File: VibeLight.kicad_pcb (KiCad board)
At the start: 2 copper layers, 29 x 34 mm, 36 parts, among them SW1 SW_Push, SW2 SW_Push, U2 SPV08A0LR5H-1, U3 BL652

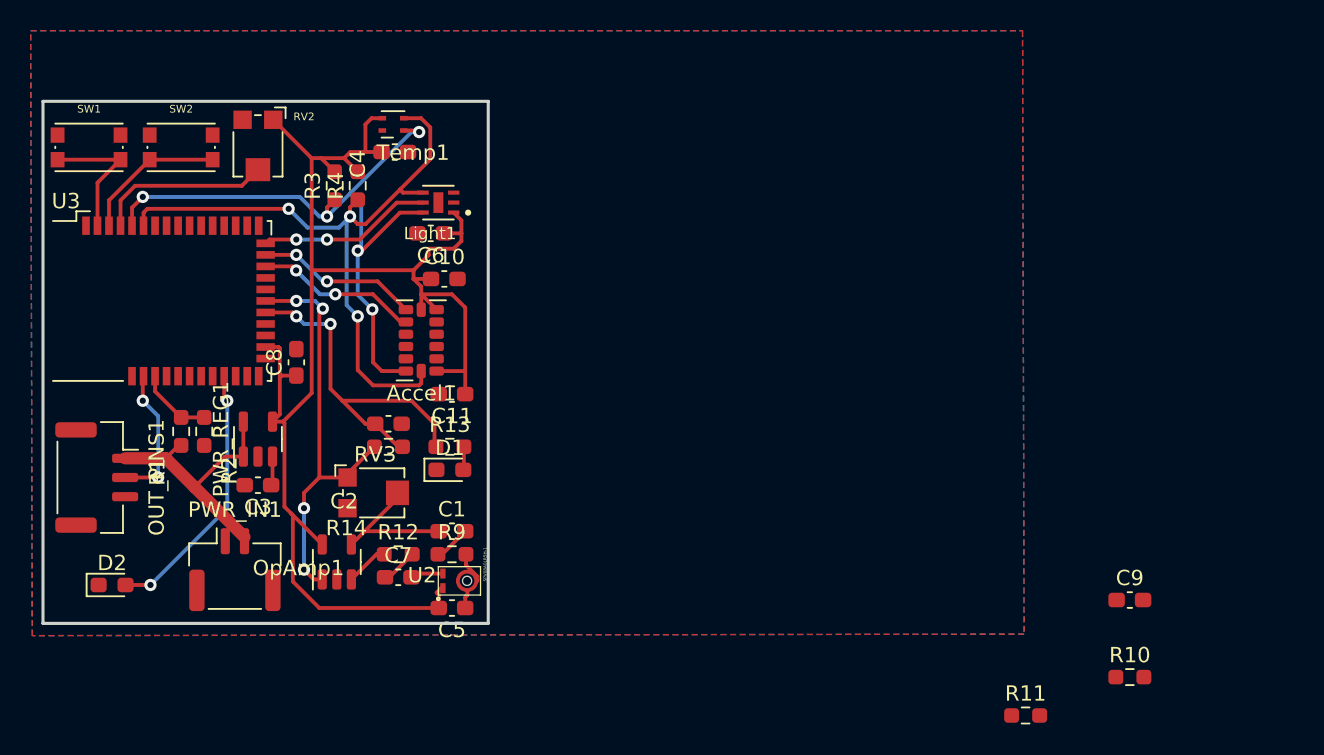
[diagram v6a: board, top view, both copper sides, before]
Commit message: new pcb rev with updated audio filter
The only ERC and DRC warnings/errors are unconnected pins and silkscreen text issues. There are two DRC issues that have to do with the mic, but I don't think they're an issue
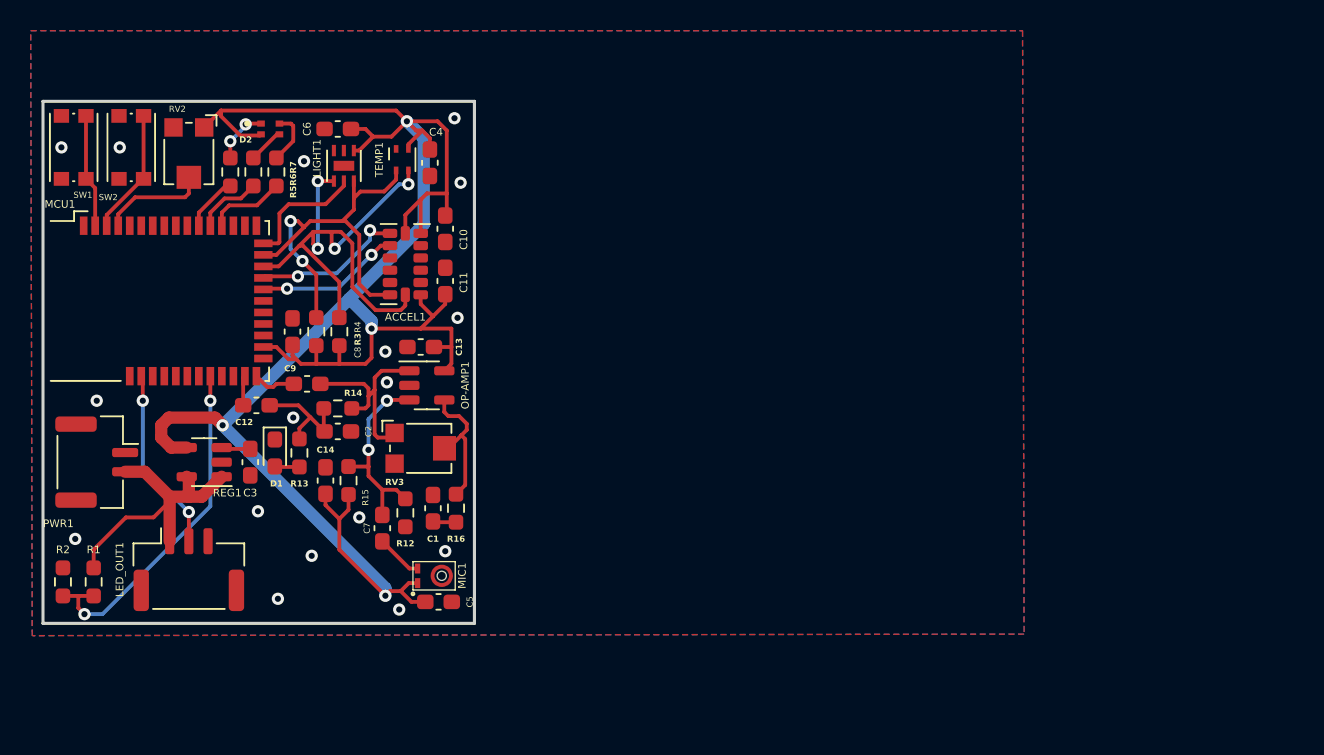
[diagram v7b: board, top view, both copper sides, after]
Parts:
- removed OpAmp1: AD8603, Package_TO_SOT_SMD:TSOT-23-5
- removed R10, R11: 10K, Resistor_SMD:R_0603_1608Metric_Pad0.98x0.95mm_HandSolder
- removed R9: R, Resistor_SMD:R_0603_1608Metric_Pad0.98x0.95mm_HandSolder
- removed U2: SPV08A0LR5H-1, MEMS_Mic_SMD:SPV08A0LR5H-1
- added C12: 100 nF, Capacitor_SMD:C_0603_1608Metric_Pad1.08x0.95mm_HandSolder, F.Cu at (31.9, 38.8)
- added C13: 100 nF, Capacitor_SMD:C_0603_1608Metric_Pad1.08x0.95mm_HandSolder, F.Cu at (42.6, 35.0)
- added C14: 100 nF, Capacitor_SMD:C_0603_1608Metric_Pad1.08x0.95mm_HandSolder, F.Cu at (36.4, 43.7)
- added MIC1: SPV08A0LR5H-1, MEMS_Mic_SMD:SPV08A0LR5H-1, F.Cu at (44.0, 49.9)
- added OP-AMP1: AD8603, Package_TO_SOT_SMD:TSOT-23-5, F.Cu at (43.0, 37.5)
- added R15: 10K, Resistor_SMD:R_0603_1608Metric_Pad0.98x0.95mm_HandSolder, F.Cu at (37.9, 43.7)
- added R16: 10K, Resistor_SMD:R_0603_1608Metric_Pad0.98x0.95mm_HandSolder, F.Cu at (44.9, 45.5)
- added R5: 100R, Resistor_SMD:R_0603_1608Metric_Pad0.98x0.95mm_HandSolder, F.Cu at (30.2, 23.6)
- added R6: 100R, Resistor_SMD:R_0603_1608Metric_Pad0.98x0.95mm_HandSolder, F.Cu at (31.7, 23.6)
- added R7: 100R, Resistor_SMD:R_0603_1608Metric_Pad0.98x0.95mm_HandSolder, F.Cu at (33.2, 23.6)
- C1: value C -> 100 nF
- C7: value 4.7uF -> 1 uF
- C9: value 1uF -> 100 nF
- D2: value LED -> LED_RBAG; footprint LED_SMD:LED_0603_1608Metric_Pad1.05x0.95mm_HandSolder -> RBG_LED:LED_APHB1608LZGKSURKC
- R12: value 4.7K -> 10K
- R13: value 60R -> 100R
- moved C9 55.4 mm to (35.2, 37.4), turned to 180 degrees
- moved D2 31.4 mm to (32.8, 20.8)
- moved R2 13.4 mm to (19.3, 50.3), turned to 90 degrees
- moved D1 11.5 mm to (33.1, 41.9), turned to -90 degrees
- moved PWR1 11.4 mm to (21.5, 42.5), turned to -90 degrees
- moved R1 11.3 mm to (21.3, 50.3), turned to -90 degrees
- moved R13 9.81 mm to (34.7, 41.9), turned to -90 degrees
- moved R3 9.58 mm to (35.8, 34.0), turned to -90 degrees
- moved R4 9.58 mm to (37.3, 34.0), turned to -90 degrees
- moved C6 9.10 mm to (37.2, 20.8)
- moved LED_OUT1 8.49 mm to (27.5, 49.5), turned to 0 degrees
- moved C11 7.38 mm to (44.2, 30.7), turned to 90 degrees
- moved LIGHT1 6.60 mm to (37.6, 23.2), turned to -90 degrees
- moved ACCEL1 5.08 mm to (41.6, 29.6)
- moved RV2 4.53 mm to (27.5, 22.5)
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- renumbered Accel1 to ACCEL1, OUT_PINS1 to LED_OUT1, Light1 to LIGHT1, U3 to MCU1, PWR_IN1 to PWR1, PWR_REG1 to REG1, Temp1 to TEMP1
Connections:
- C1 pad 1: Net-(OpAmp1--) -> GND
- C2 pad 2: /Audio Input/FIL -> Net-(C12-Pad1)
- C7 pad 1: Net-(C7-Pad1) -> Net-(OP-AMP1-+)
- C9 pad 1: GND -> Net-(C9-Pad1)
- C9 pad 2: Net-(OpAmp1-+) -> /Audio Input/RAW
- D2 pad 1: GND -> Net-(D2-RK)
- D2 pad 2: /MCU/BATT_LVL -> Net-(D2-BK)
- MCU1 pad 11: unconnected-(U3-SIO_14-Pad11) -> Net-(MCU1-SIO_14)
- MCU1 pad 12: unconnected-(U3-SIO_12-Pad12) -> Net-(MCU1-SIO_12)
- MCU1 pad 13: unconnected-(U3-SIO_11-Pad13) -> Net-(MCU1-SIO_11)
- MCU1 pad 18: /MCU/ACC_INT1 -> /SDA
- MCU1 pad 19: /MCU/ACC_INT2 -> /SCL
- MCU1 pad 20: unconnected-(U3-SIO_05/AIN3-Pad20) -> /MCU/ACC_INT1
- MCU1 pad 21: unconnected-(U3-SIO_04/AIN2-Pad21) -> /MCU/ACC_INT2
- MCU1 pad 22: /Audio Input/RAW -> unconnected-(MCU1-SIO_03/AIN1-Pad22)
- MCU1 pad 23: /Audio Input/FIL -> unconnected-(MCU1-SIO_02/AIN0-Pad23)
- MCU1 pad 28: unconnected-(U3-SIO_13-Pad28) -> /Audio Input/RAW
- MCU1 pad 29: unconnected-(U3-SIO_15-Pad29) -> /Audio Input/FIL
- MCU1 pad 31: /MCU/BATT_LVL -> unconnected-(MCU1-SIO_19-Pad31)
- MCU1 pad 32: unconnected-(U3-SIO_31/AIN7-Pad32) -> Net-(MCU1-SIO_31/AIN7)
- MCU1 pad 37: Net-(U3-SIO_26) -> unconnected-(MCU1-SIO_26-Pad37)
- MCU1 pad 5: /SDA -> unconnected-(MCU1-SWDIO-Pad5)
- MCU1 pad 6: /SCL -> unconnected-(MCU1-SWDCLK-Pad6)
- R1 pad 2: Net-(U3-SIO_26) -> Net-(MCU1-SIO_31/AIN7)
- R12 pad 1: Net-(OpAmp1-+) -> Net-(OP-AMP1-+)
- R12 pad 2: Net-(C7-Pad1) -> GND
- R13 pad 1: /Audio Input/FIL -> Net-(C12-Pad1)
- R14 pad 1: /Audio Input/RAW -> Net-(C9-Pad1)
- R14 pad 2: /Audio Input/FIL -> Net-(C12-Pad1)
- R2 pad 1: Net-(U3-SIO_26) -> Net-(MCU1-SIO_31/AIN7)
- RV3 pad 1: /Audio Input/RAW -> Net-(C9-Pad1)
- RV3 pad 2: Net-(OpAmp1--) -> Net-(OP-AMP1--)
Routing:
- net +3V3: track 94.9 -> 134.9 mm, vias 0 -> 4
- net /Audio Input/RAW: track 27.5 -> 2.81 mm, vias 4 -> 0
- net Net-(MCU1-SIO_31/AIN7): track 0.00 -> 22.9 mm, vias 0 -> 2
- net /Audio Input/FIL: track 23.2 -> 1.95 mm, vias 2 -> 0
- net /MCU/BATT_LVL: track 17.4 -> 0.00 mm, vias 2 -> 0
- net /SDA: track 44.8 -> 27.8 mm, vias 5 -> 2
- net Net-(C9-Pad1): track 0.00 -> 13.8 mm
- net Net-(OP-AMP1-+): track 0.00 -> 12.8 mm, vias 0 -> 2
- net Net-(OpAmp1--): track 9.43 -> 0.00 mm
- net /SCL: track 45.1 -> 36.0 mm, vias 3 -> 4
- net Net-(OP-AMP1--): track 0.00 -> 9.10 mm
- net Net-(C12-Pad1): track 0.00 -> 7.50 mm
- net Net-(MCU1-SIO_11): track 0.00 -> 5.12 mm
- net Net-(U3-SIO_26): track 4.89 -> 0.00 mm
- net /MCU/Intensity_Dial: track 11.4 -> 6.96 mm
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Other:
- board size 29 x 34 mm -> 28.1 x 34 mm

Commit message: Misc updates and tweak. Work still needed, letf notes in top schematic page
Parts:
- added J1: Conn_ARM_SWD_TagConnect_TC2030-NL, Connector:Tag-Connect_TC2030-IDC-NL_2x03_P1.27mm_Vertical, B.Cu at (27.6, 31.5)
- R1, R2: value R -> 100K
- moved R1 2.86 mm to (20.4, 47.6), turned to 180 degrees
- moved C14 2.59 mm to (36.1, 46.3)
- moved R15 2.59 mm to (37.6, 46.3)
- moved C8 2.47 mm to (36.5, 35.0), turned to 180 degrees
- moved C4 2.37 mm to (41.0, 22.2), turned to 180 degrees
- moved D1 2.18 mm to (34.3, 43.7), turned to 180 degrees
- moved TEMP1 1.70 mm to (40.6, 24.3)
- moved C11 1.68 mm to (44.2, 32.4)
- moved R3 1.68 mm to (35.8, 32.3)
- moved R4 1.68 mm to (37.3, 32.3)
- moved C10 1.64 mm to (43.6, 25.8), turned to 0 degrees
- moved R2 1.47 mm to (20.4, 49.3), turned to 0 degrees
- moved R13 0.44 mm to (34.3, 42.1), turned to 180 degrees
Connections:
- MCU1 pad 28: /Audio Input/RAW -> unconnected-(MCU1-SIO_13-Pad28)
- MCU1 pad 29: /Audio Input/FIL -> unconnected-(MCU1-SIO_15-Pad29)
- MCU1 pad 4: /MCU/Intensity_Dial -> unconnected-(MCU1-SIO_22-Pad4)
- MCU1 pad 5: unconnected-(MCU1-SWDIO-Pad5) -> /MCU/SWDIO
- MCU1 pad 6: unconnected-(MCU1-SWDCLK-Pad6) -> /MCU/SWCLK
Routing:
- net +3V3: track 134.9 -> 118.9 mm
- net /MCU/Intensity_Dial: track 6.96 -> 0.00 mm
- net GND: track 0.00 -> 3.64 mm, vias 17 -> 22
- net /SDA: track 27.8 -> 24.4 mm
- net /SCL: track 36.0 -> 32.9 mm
- net /Audio Input/RAW: track 2.81 -> 0.00 mm
- net /BATT+: track 19.5 -> 17.2 mm
- net /Audio Input/FIL: track 1.95 -> 0.00 mm
- net Net-(OP-AMP1-+): track 12.8 -> 14.0 mm
- net Net-(MCU1-SIO_31/AIN7): track 22.9 -> 22.4 mm
